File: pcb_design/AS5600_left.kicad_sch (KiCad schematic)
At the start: 5 parts, among them IC1 AS5600-ASOT, J4 AS5600_Left

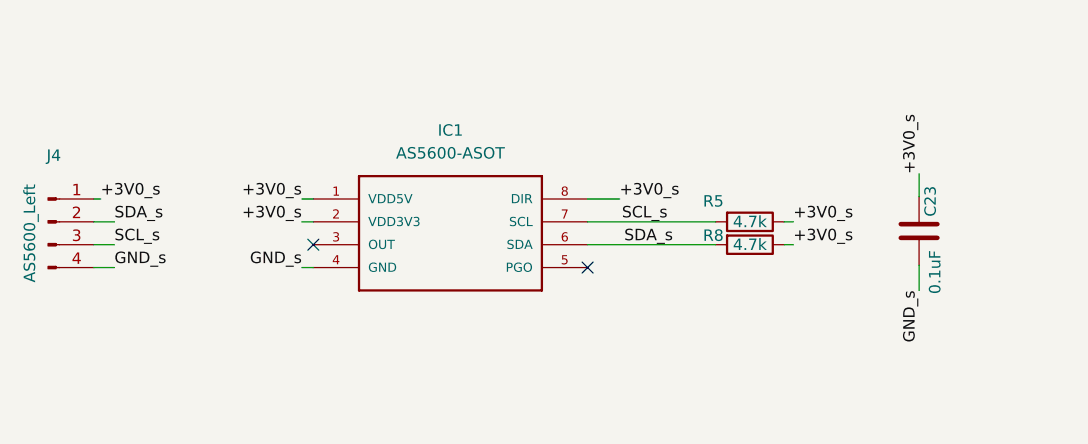
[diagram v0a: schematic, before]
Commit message: changed AS5600 to AS5048B
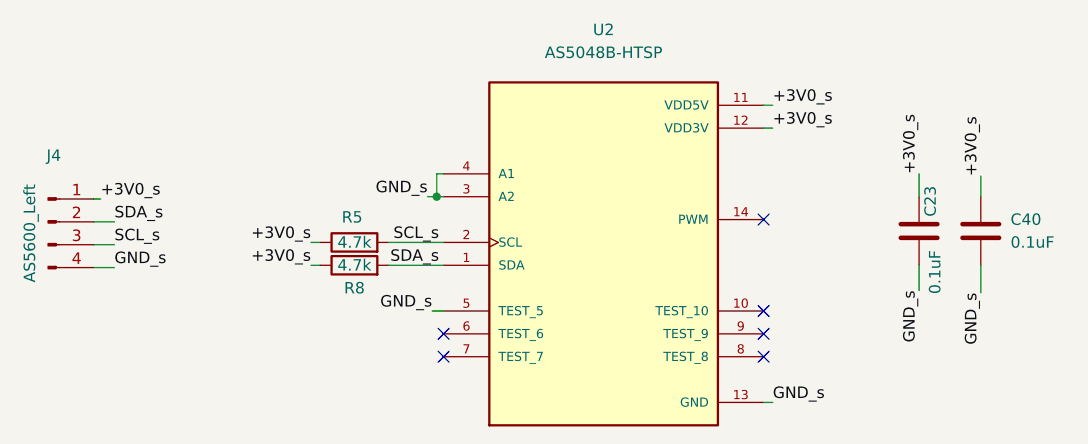
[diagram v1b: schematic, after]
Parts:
- removed IC1: AS5600-ASOT, AS5600-ASOT:SOIC127P600X175-8N, symbol AS5600-ASOT:AS5600-ASOT
- added C40: 0.1uF, Capacitor_SMD:C_0402_1005Metric, symbol Device:C
- added U2: AS5048B-HTSP, AS5048B-HTSP:SOP65P640X120-14N, symbol AS5048B-HTSP:AS5048B-HTSP
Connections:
- net +3V0_s: now also C40.1, U2.11 (VDD5V), U2.12 (VDD3V)
- net GND_s: now also C40.2, U2.13 (GND), U2.3 (A2), U2.4 (A1), U2.5 (TEST_5)
- net SCL_s: now also R5.2, U2.2 (SCL); no longer R8.2
- net SDA_s: now also R8.2, U2.1 (SDA); no longer R5.2
- no-connect marks 2 -> 6

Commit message: modified capacitors for encoders
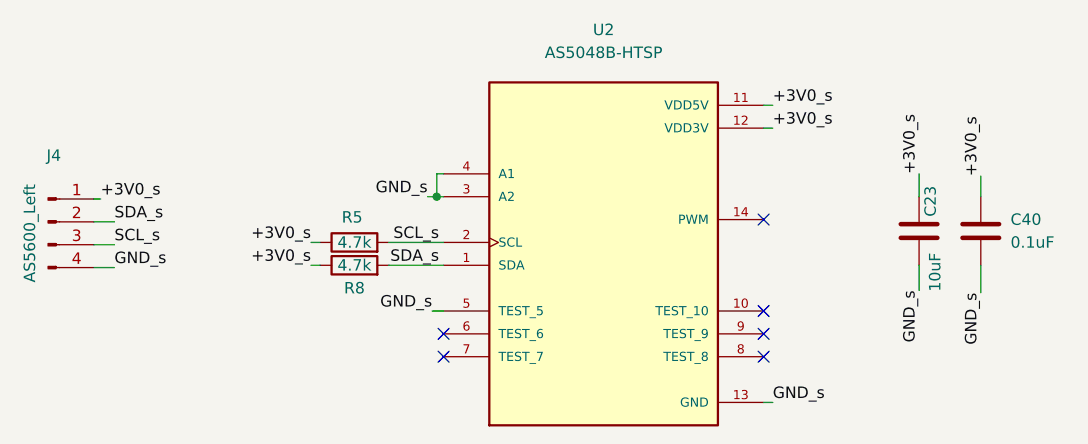
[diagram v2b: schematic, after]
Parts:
- C23: value 0.1uF -> 10uF; footprint Capacitor_SMD:C_0402_1005Metric -> Capacitor_SMD:C_0603_1608Metric
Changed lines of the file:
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@@
     (in_bom yes) (on_board yes)
     (property "Reference" "C23" (id 0) (at 208.28 92.964 90))
-    (property "Value" "0.1uF" (id 1) (at 208.788 100.838 90))
-    (property "Footprint" "Capacitor_SMD:C_0402_1005Metric" (id 2) (at 206.0448 92.456 0)
+    (property "Value" "10uF" (id 1) (at 208.788 100.838 90))
+    (property "Footprint" "Capacitor_SMD:C_0603_1608Metric" (id 2) (at 206.0448 92.456 0)
       (effects (font (size 1.27 1.27)) hide)
     )
